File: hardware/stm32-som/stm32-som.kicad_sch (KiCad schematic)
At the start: 5 parts

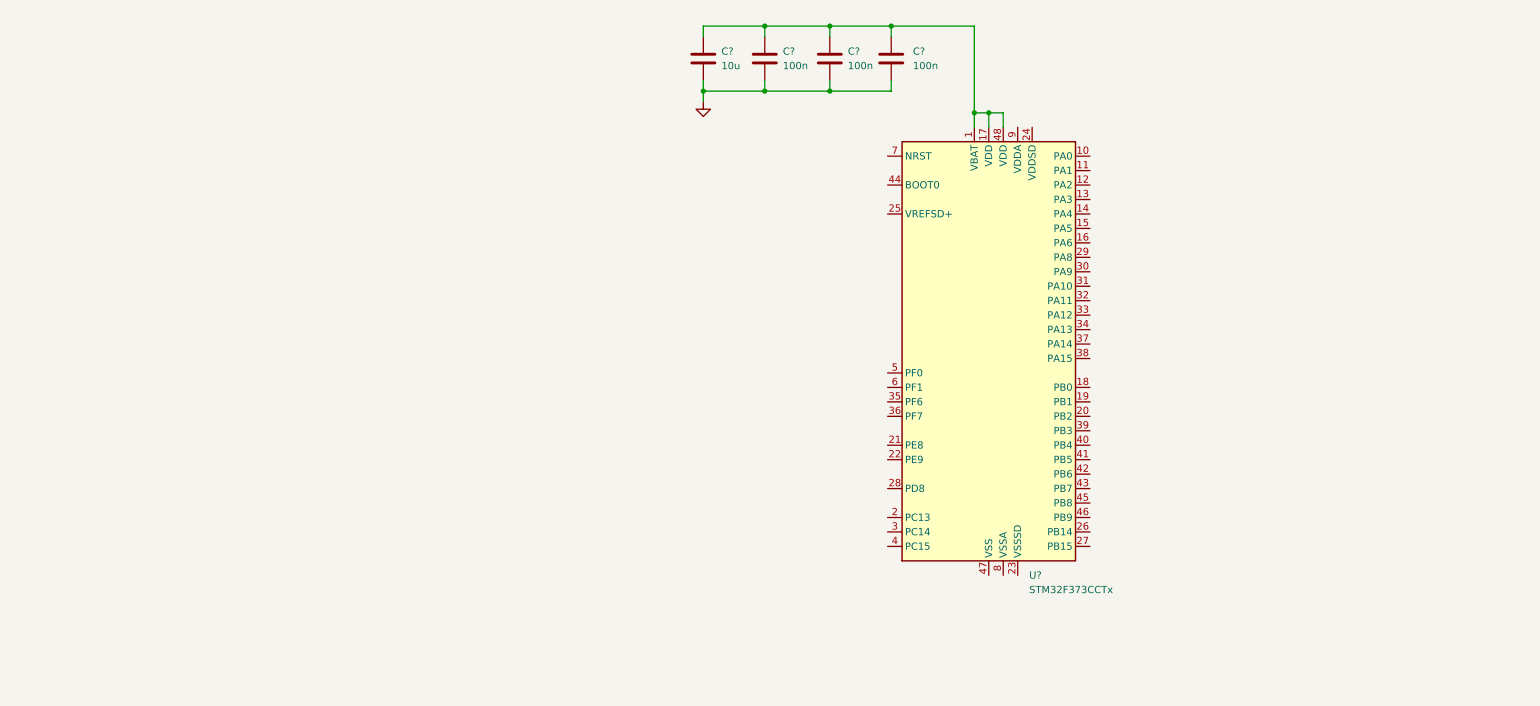
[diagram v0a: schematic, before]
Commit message: add power supply to som, change MCU to STM32F412RE, draw MCU schematic layer
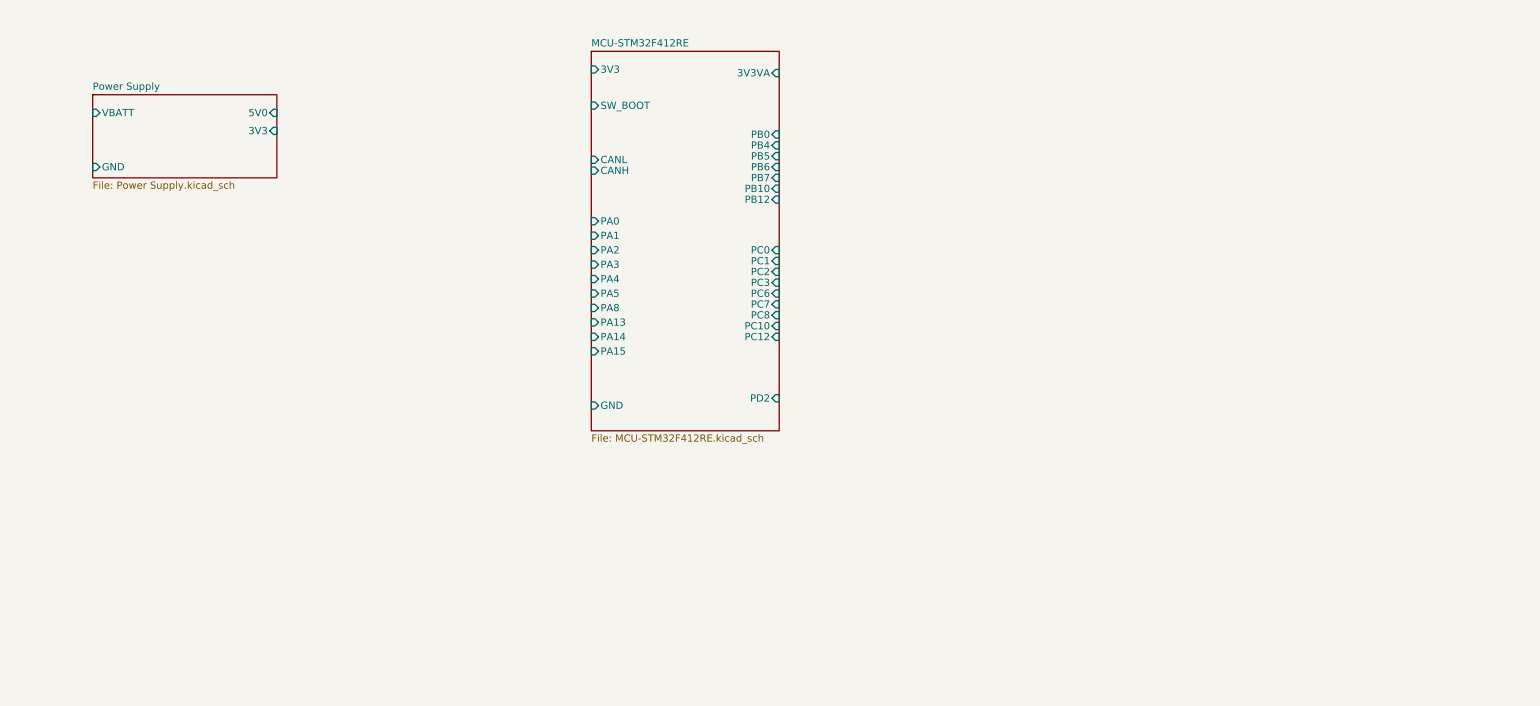
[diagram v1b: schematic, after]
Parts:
- removed C? (x3): 100n, symbol Device:C
- removed C?: 10u, symbol Device:C
- removed U?: STM32F373CCTx, Package_QFP:LQFP-48_7x7mm_P0.5mm, symbol MCU_ST_STM32F3:STM32F373CCTx
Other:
- added sheet MCU-STM32F412RE (MCU-STM32F412RE.kicad_sch)
- added sheet Power Supply (Power Supply.kicad_sch)

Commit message: add test points, complete top hierarchical level, correct jtag mcu connection
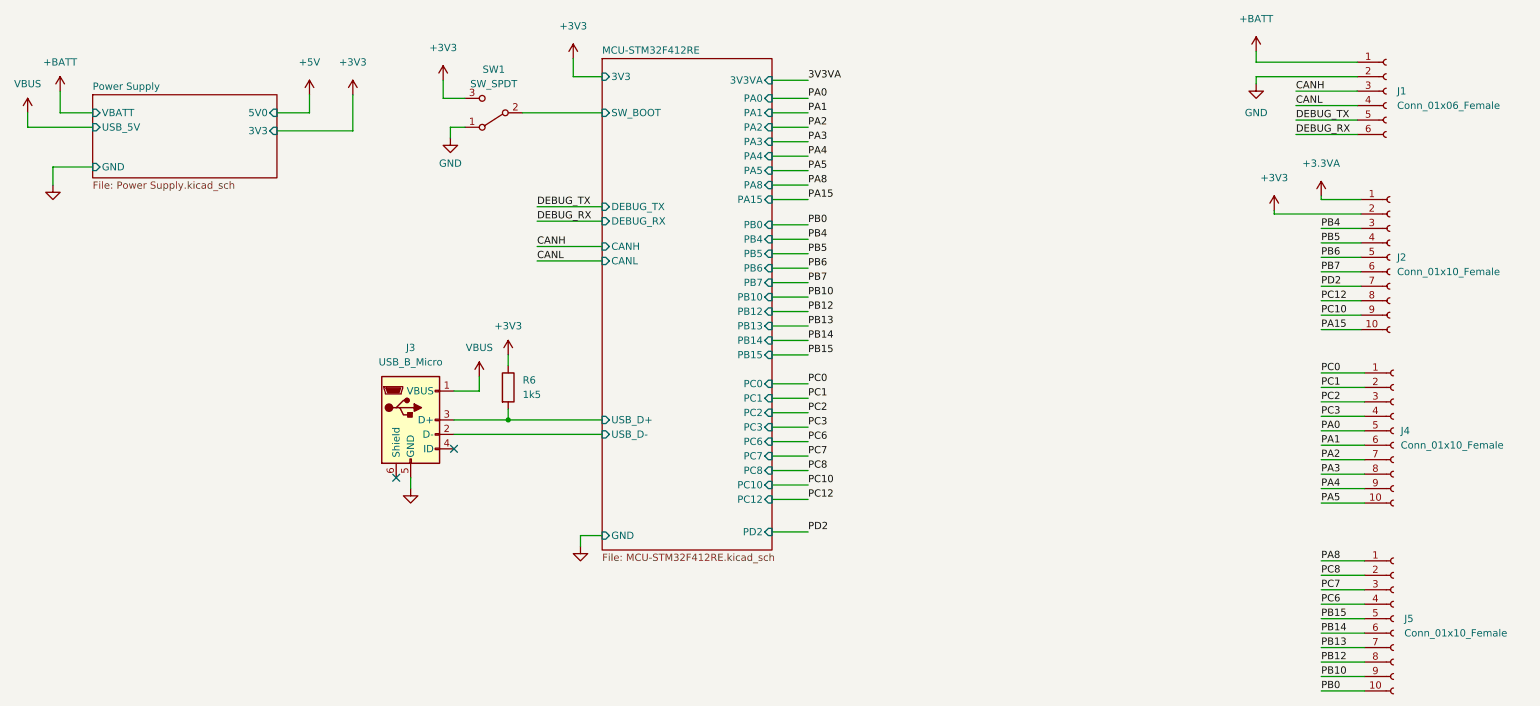
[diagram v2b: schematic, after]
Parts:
- added J1: Conn_01x06_Female, symbol Connector:Conn_01x06_Female
- added J2, J4, J5: Conn_01x10_Female, symbol Connector:Conn_01x10_Female
- added J3: USB_B_Micro, symbol Connector:USB_B_Micro
- added R6: 1k5, symbol Device:R
- added SW1: SW_SPDT, symbol Switch:SW_SPDT
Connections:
- net MCU-STM32F412RE/SW_BOOT: now also SW1.2 (B)
- new net +3.3VA: J2.1 (Pin_1)
- new net +3V3: J2.2 (Pin_2), R6.1, SW1.3 (C)
- new net +BATT: J1.1 (Pin_1)
- new net CANH: J1.3 (Pin_3)
- new net CANL: J1.4 (Pin_4)
- new net DEBUG_RX: J1.6 (Pin_6)
- new net DEBUG_TX: J1.5 (Pin_5)
- new net GND: J1.2 (Pin_2), J3.5 (GND), SW1.1 (A)
- new net MCU-STM32F412RE/USB_D+: J3.3 (D+), R6.2
- new net MCU-STM32F412RE/USB_D-: J3.2 (D-)
- new net PA0: J4.5 (Pin_5)
- new net PA1: J4.6 (Pin_6)
- new net PA15: J2.10 (Pin_10)
- new net PA2: J4.7 (Pin_7)
- new net PA3: J4.8 (Pin_8)
- new net PA4: J4.9 (Pin_9)
- new net PA5: J4.10 (Pin_10)
- new net PA8: J5.1 (Pin_1)
- new net PB0: J5.10 (Pin_10)
- new net PB10: J5.9 (Pin_9)
- new net PB12: J5.8 (Pin_8)
- new net PB13: J5.7 (Pin_7)
- new net PB14: J5.6 (Pin_6)
- new net PB15: J5.5 (Pin_5)
- new net PB4: J2.3 (Pin_3)
- new net PB5: J2.4 (Pin_4)
- new net PB6: J2.5 (Pin_5)
- new net PB7: J2.6 (Pin_6)
- new net PC0: J4.1 (Pin_1)
- new net PC1: J4.2 (Pin_2)
- new net PC10: J2.9 (Pin_9)
- new net PC12: J2.8 (Pin_8)
- new net PC2: J4.3 (Pin_3)
- new net PC3: J4.4 (Pin_4)
- new net PC6: J5.4 (Pin_4)
- new net PC7: J5.3 (Pin_3)
- new net PC8: J5.2 (Pin_2)
- new net PD2: J2.7 (Pin_7)
- new net VBUS: J3.1 (VBUS)
- no-connect marks 0 -> 2
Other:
- sheet MCU-STM32F412RE ports: added DEBUG_RX, DEBUG_TX, PB13, PB14, PB15, USB_D+, USB_D-; removed PA13, PA14
- sheet Power Supply ports: added USB_5V; removed none

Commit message: clear ERC, small question about voltage level and rail timing on VCAP, but otherwise net name stuff
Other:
- sheet MCU-STM32F412RE ports: added +3.3VA, +3V3; removed 3V3, 3V3VA
- sheet Power Supply ports: added +3V3, +5V, +BATT; removed 3V3, 5V0, VBATT
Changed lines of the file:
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@@
     (company "Flyover Embedded")
+  )
+  (junction (at 247.015 22.86) (diameter 0) (color 0 0 0 0)
   )
   (junction (at 104.775 85.725) (diameter 0) (color 0 0 0 0)
@@
     (stroke (width 0) (type default) (color 0 0 0 0))
   )
+  (wire (pts (xy 247.015 22.86) (xy 254 22.86))
+    (stroke (width 0) (type default) (color 0 0 0 0))
+  )
   (wire (pts (xy 151.13 79.375) (xy 157.48 79.375))
     (stroke (width 0) (type default) (color 0 0 0 0))
@@
     (stroke (width 0) (type default) (color 0 0 0 0))
   )
+  (wire (pts (xy 247.015 20.955) (xy 247.015 22.86))
+    (stroke (width 0) (type default) (color 0 0 0 0))
+  )
   (wire (pts (xy 151.13 34.29) (xy 157.48 34.29))
     (stroke (width 0) (type default) (color 0 0 0 0))
@@
     (stroke (width 0) (type default) (color 0 0 0 0))
   )
-  (wire (pts (xy 236.22 22.86) (xy 254 22.86))
+  (wire (pts (xy 236.22 22.86) (xy 247.015 22.86))
     (stroke (width 0) (type default) (color 0 0 0 0))
   )
@@
   (label "PC12" (at 157.48 99.695 0)
     (effects (font (size 1.27 1.27)) (justify left bottom))
+  )
+  (symbol (lib_id "power:PWR_FLAG") (at 247.015 20.955 0) (unit 1)
+    (in_bom yes) (on_board yes) (fields_autoplaced)
+    (property "Reference" "#FLG0101" (id 0) (at 247.015 19.05 0)
+      (effects (font (size 1.27 1.27)) hide)
+    )
+    (property "Value" "PWR_FLAG" (id 1) (at 247.015 15.24 0))
+    (property "Footprint" "" (id 2) (at 247.015 20.955 0)
+      (effects (font (size 1.27 1.27)) hide)
+    )
+    (property "Datasheet" "~" (id 3) (at 247.015 20.955 0)
+      (effects (font (size 1.27 1.27)) hide)
+    )
+    (pin "1")
   )
   (symbol (lib_id "power:+3V3") (at 77.47 28.575 0) (unit 1)
@@
       (effects (font (size 1.27 1.27)) (justify right))
     )
-    (pin "3V3" input (at 121.285 25.4 180)
-      (effects (font (size 1.27 1.27)) (justify left))
-    )
-    (pin "3V3VA" input (at 151.13 26.035 0)
+    (pin "+3V3" input (at 121.285 25.4 180)
+      (effects (font (size 1.27 1.27)) (justify left))
+    )
+    (pin "+3.3VA" input (at 151.13 26.035 0)
       (effects (font (size 1.27 1.27)) (justify right))
     )
@@
       (effects (font (size 1.27 1.27)) (justify left top))
     )
-    (pin "VBATT" input (at 31.75 31.75 180)
+    (pin "+BATT" input (at 31.75 31.75 180)
       (effects (font (size 1.27 1.27)) (justify left))
     )
@@
       (effects (font (size 1.27 1.27)) (justify left))
     )
-    (pin "5V0" input (at 64.135 31.75 0)
-      (effects (font (size 1.27 1.27)) (justify right))
-    )
-    (pin "3V3" input (at 64.135 34.925 0)
+    (pin "+5V" input (at 64.135 31.75 0)
+      (effects (font (size 1.27 1.27)) (justify right))
+    )
+    (pin "+3V3" input (at 64.135 34.925 0)
       (effects (font (size 1.27 1.27)) (justify right))
     )
@@
   )
   (symbol_instances
+    (path "/01250b99-346a-47eb-99f4-0af205a8c683"
+      (reference "#FLG0101") (unit 1) (value "PWR_FLAG") (footprint "")
+    )
+    (path "/935760a4-2e21-49e5-b565-e9c8972093d7/934aba78-62c6-4b1b-b2e3-1097b2444b7f"
+      (reference "#FLG0102") (unit 1) (value "PWR_FLAG") (footprint "")
+    )
+    (path "/935760a4-2e21-49e5-b565-e9c8972093d7/679064c4-d1a0-4e79-9656-e036dbb547d7"
+      (reference "#FLG0103") (unit 1) (value "PWR_FLAG") (footprint "")
+    )
+    (path "/8cc0665d-0821-42e9-b2d5-9f56f7ddf764/2b08ab8f-574f-42b8-b468-a7a07de4ccc8"
+      (reference "#FLG0104") (unit 1) (value "PWR_FLAG") (footprint "")
+    )
+    (path "/935760a4-2e21-49e5-b565-e9c8972093d7/37bab2d8-3da0-4710-adf7-a93b7052105c"
+      (reference "#FLG0105") (unit 1) (value "PWR_FLAG") (footprint "")
+    )
+    (path "/8cc0665d-0821-42e9-b2d5-9f56f7ddf764/d4af2995-230c-4abe-81fd-9ee7498e6b8a"
+      (reference "#FLG0106") (unit 1) (value "PWR_FLAG") (footprint "")
+    )
     (path "/935760a4-2e21-49e5-b565-e9c8972093d7/6e67d1a6-231e-447b-bafa-57fe7b283b31"
       (reference "#PWR01") (unit 1) (value "+BATT") (footprint "")
@@
       (reference "#PWR050") (unit 1) (value "GND") (footprint "")
     )
+    (path "/8cc0665d-0821-42e9-b2d5-9f56f7ddf764/ce038734-9a74-436a-b55a-7398c385da40"
+      (reference "#PWR0101") (unit 1) (value "GND") (footprint "")
+    )
     (path "/935760a4-2e21-49e5-b565-e9c8972093d7/04ad67d2-085e-421c-9c88-48b09f0e20d5"

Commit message: add footprints to all components, JLC part numbers to to everything except capacitors and resistors
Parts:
- J1: footprint (none) -> custom-footprints:1x6p-2.54mm-castellated
- J2, J4, J5: footprint (none) -> custom-footprints:1x10p-2.54mm-castellated
- J3: footprint (none) -> Connector_USB:USB_Micro-B_Amphenol_10118194_Horizontal; JLC (none) -> C132563
- R6: footprint (none) -> Resistor_SMD:R_0402_1005Metric
- SW1: footprint (none) -> Button_Switch_SMD:SW_SPDT_PCM12

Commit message: swap big qspi test points for small test header, complete rough layout
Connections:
- net CANH: now also J1.4 (Pin_4); no longer J1.3 (Pin_3)
- net CANL: now also J1.3 (Pin_3); no longer J1.4 (Pin_4)
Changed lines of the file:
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@@
     (effects (font (size 1.27 1.27)) (justify left bottom))
   )
-  (label "CANH" (at 243.205 27.94 0)
+  (label "CANH" (at 243.205 30.48 0)
     (effects (font (size 1.27 1.27)) (justify left bottom))
   )
@@
     (effects (font (size 1.27 1.27)) (justify left bottom))
   )
-  (label "CANL" (at 243.205 30.48 0)
+  (label "CANL" (at 243.205 27.94 0)
     (effects (font (size 1.27 1.27)) (justify left bottom))
   )
@@
       (reference "J6") (unit 1) (value "TC2030") (footprint "Connector:Tag-Connect_TC2030-IDC-FP_2x03_P1.27mm_Vertical")
     )
+    (path "/8cc0665d-0821-42e9-b2d5-9f56f7ddf764/28d87406-1f25-4632-b32f-a4a373f2109d"
+      (reference "J7") (unit 1) (value "Conn_02x03_Counter_Clockwise") (footprint "Connector_PinHeader_1.27mm:PinHeader_2x03_P1.27mm_Vertical_SMD")
+    )
     (path "/935760a4-2e21-49e5-b565-e9c8972093d7/3cf61ff5-d001-475a-828e-af303e9ca3fc"
       (reference "JP1") (unit 1) (value "SolderJumper_3_Bridged12") (footprint "Jumper:SolderJumper-3_P1.3mm_Bridged12_Pad1.0x1.5mm_NumberLabels")
@@
       (reference "TP6") (unit 1) (value "TestPoint") (footprint "TestPoint:TestPoint_Loop_D2.54mm_Drill1.5mm_Beaded")
     )
-    (path "/8cc0665d-0821-42e9-b2d5-9f56f7ddf764/8debcdc3-0828-4fd7-a9ed-63cbe6bf96ac"
-      (reference "TP7") (unit 1) (value "TestPoint") (footprint "TestPoint:TestPoint_Loop_D2.54mm_Drill1.5mm_Beaded")
-    )
-    (path "/8cc0665d-0821-42e9-b2d5-9f56f7ddf764/c4e28d4f-d902-439b-912b-28b0a07b94ca"
-      (reference "TP8") (unit 1) (value "TestPoint") (footprint "TestPoint:TestPoint_Loop_D2.54mm_Drill1.5mm_Beaded")
-    )
-    (path "/8cc0665d-0821-42e9-b2d5-9f56f7ddf764/bfaf6999-4028-4729-ab6a-f20b81c5b811"
-      (reference "TP9") (unit 1) (value "TestPoint") (footprint "TestPoint:TestPoint_Loop_D2.54mm_Drill1.5mm_Beaded")
-    )
-    (path "/8cc0665d-0821-42e9-b2d5-9f56f7ddf764/f465083f-e654-4ab7-a4c8-4e35a405910d"
-      (reference "TP10") (unit 1) (value "TestPoint") (footprint "TestPoint:TestPoint_Loop_D2.54mm_Drill1.5mm_Beaded")
-    )
-    (path "/8cc0665d-0821-42e9-b2d5-9f56f7ddf764/8dd9f700-1e55-4a56-a66a-bd345c013fb3"
-      (reference "TP11") (unit 1) (value "TestPoint") (footprint "TestPoint:TestPoint_Loop_D2.54mm_Drill1.5mm_Beaded")
-    )
-    (path "/8cc0665d-0821-42e9-b2d5-9f56f7ddf764/18186462-fac5-44e8-bf56-a49b410a39c5"
-      (reference "TP12") (unit 1) (value "TestPoint") (footprint "TestPoint:TestPoint_Loop_D2.54mm_Drill1.5mm_Beaded")
-    )
     (path "/8cc0665d-0821-42e9-b2d5-9f56f7ddf764/5b96dbfa-b79f-46a9-ab1d-ac48bd28ff9d"
